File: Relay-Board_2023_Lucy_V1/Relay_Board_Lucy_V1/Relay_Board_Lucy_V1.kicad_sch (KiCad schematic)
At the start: 54 parts, among them J1 VP0265540000G, J2 VP0265540000G, J3 Startup Resistor, J5 Battery Power, J9 VP0265540000G, Q1 SI2302A-TPMSCT-ND, U1 TSV914IPT, U2 ACS770LCB-050U-PFF, U3 ACS770LCB-050U-PFF, U4 ACS770LCB-050U-PFF, U6 MAX14572, U8 TSV914IPT

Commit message: Updates
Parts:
- removed J3: Startup Resistor, symbol Connector:Screw_Terminal_01x02
- added J4: VP0265540000G, RB_FTP:CONN_VP0265x4xxxxG_AMP, symbol RB_PARTS:VP0265540000G
- added NT1: NetTie_2, NetTie:NetTie-2_SMD_Pad2.0mm, symbol Device:NetTie_2
- C9: value 0u1 -> 100n; footprint (none) -> Capacitor_SMD:C_0603_1608Metric
- C9: footprint (none) -> Capacitor_SMD:C_0603_1608Metric
- D1: renamed from D2; footprint (none) -> LED_SMD:LED_0805_2012Metric
- R1: footprint (none) -> Resistor_SMD:R_0603_1608Metric
- renumbered D14 to D10, D15 to D11, D16 to D2, D1 to D3, D7 to D5, D11 to D6, D12 to D7, D13 to D9, J5 to J1, J9 to J2, J1 to J3, J2 to J5, U2 to U1, U3 to U2, U8 to U4, U1 to U5, U4 to U6
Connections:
- net GNDA: now also NT1.1
- net GNDPWR: now also J4.3, J4.4, NT1.2
- net RES+: now also J4.1, J4.2
- no-connect marks 13 -> 14

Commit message: Started the PCB design work
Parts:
- added H1, H2, H3, H4: MountingHole, MountingHole:MountingHole_3.2mm_M3, symbol Mechanical:MountingHole
- U1, U2, U6: footprint Sensor_Current:Allegro_CB_PFF -> RB_FTP:Allegro_CB_PFF_Adjusted
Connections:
- net PA0 is gone; now on net PA4: D8.3 (K), U4.8 (OUT3), U4.9 (IN3-)
- net PA1 is gone; now on net PA6: D5.3 (K), U4.6 (IN2-), U4.7 (OUT2)
- net PA2 is gone; now on net PA7: D7.3 (K), U5.6 (IN2-), U5.7 (OUT2)
- net PA3 is gone; now on net PA5: D9.3 (K), U5.8 (OUT3), U5.9 (IN3-)
- net CAP+: now also J3.3, J3.4; no longer J3.1, J3.2
- net FC+: now also J2.3, J2.4; no longer J2.1, J2.2
- net GNDA: now also C9.1, C9.2, C9.2, C9.2, C9.2, D1.1 (K), D2.3 (K), J1.2 (Pin_2), J1.5 (Pin_5), R1.1, R1.1, R1.1, U1.2 (GND), U2.2 (GND), U6.15 (EP), U6.2 (GND), U6.7 (GND), U6.8 (~{HVEN})
- net GNDPWR: now also J2.1, J2.2, J3.1, J3.2, J5.1, J5.2; no longer C9.1, C9.2, C9.2, C9.2, C9.2, D1.1 (K), D2.3 (K), J1.2 (Pin_2), J1.5 (Pin_5), J2.3, J2.4, J3.3, J3.4, J5.3, J5.4, R1.1, R1.1, R1.1, U1.2 (GND), U2.2 (GND), U6.15 (EP), U6.2 (GND), U6.7 (GND), U6.8 (~{HVEN})
- net MOTOR+: now also J5.3, J5.4; no longer J5.1, J5.2
- net PA4: no longer D6.3 (K), U5.1 (OUT1), U5.2 (IN1-)
- net PB0: no longer R1.1
- net PB1: no longer R1.2
- net PB2: no longer R1.1
- net PA9 renamed PC4
- net PB3 renamed PB15
- new net PB12: R1.1
- new net PB13: R1.2
- new net PB14: R1.1
- new net PC5: D6.3 (K), U5.1 (OUT1), U5.2 (IN1-)
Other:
- moved on the sheet: C9, D1, D2, J2, J3, Q1, R1, U6

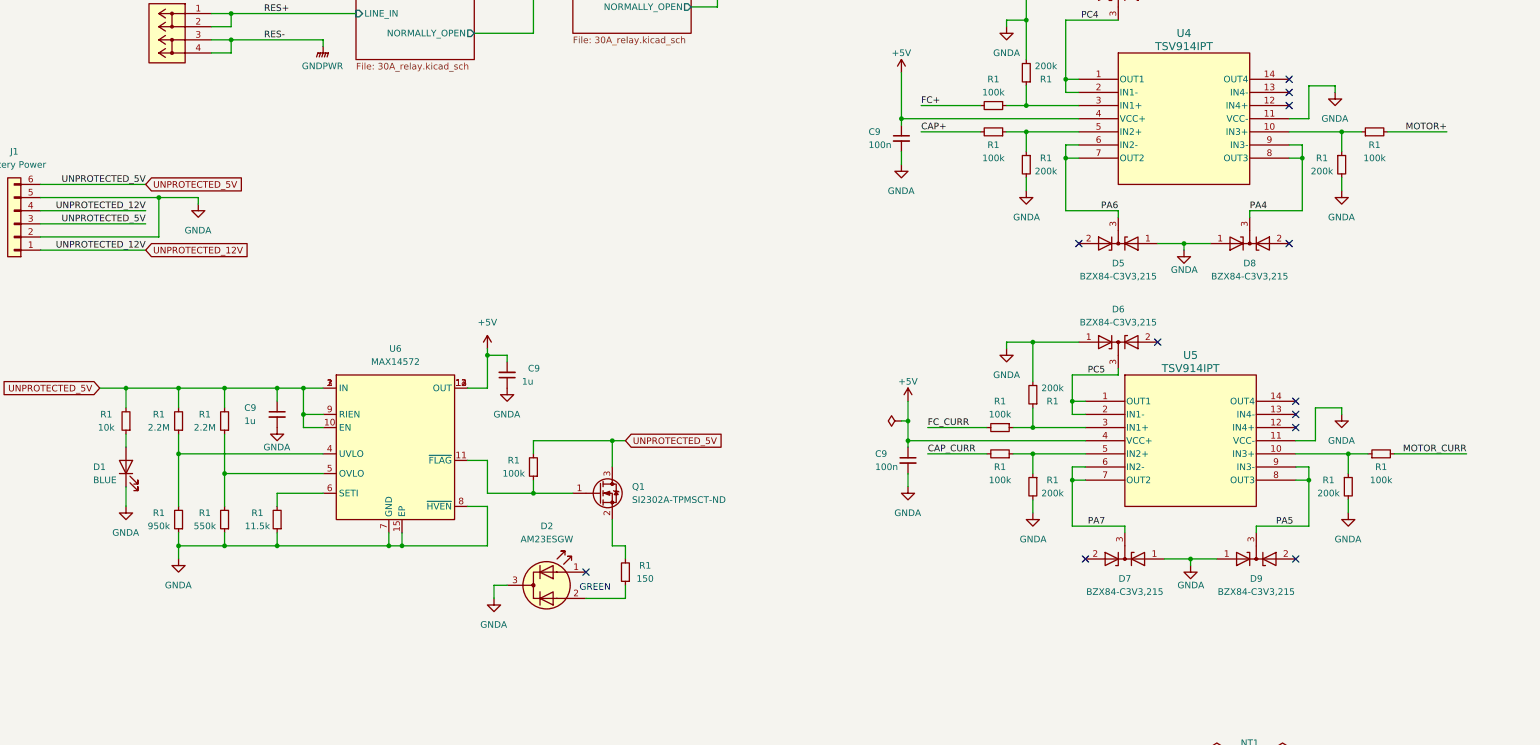
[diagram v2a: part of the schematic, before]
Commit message: Board layout is done and routed
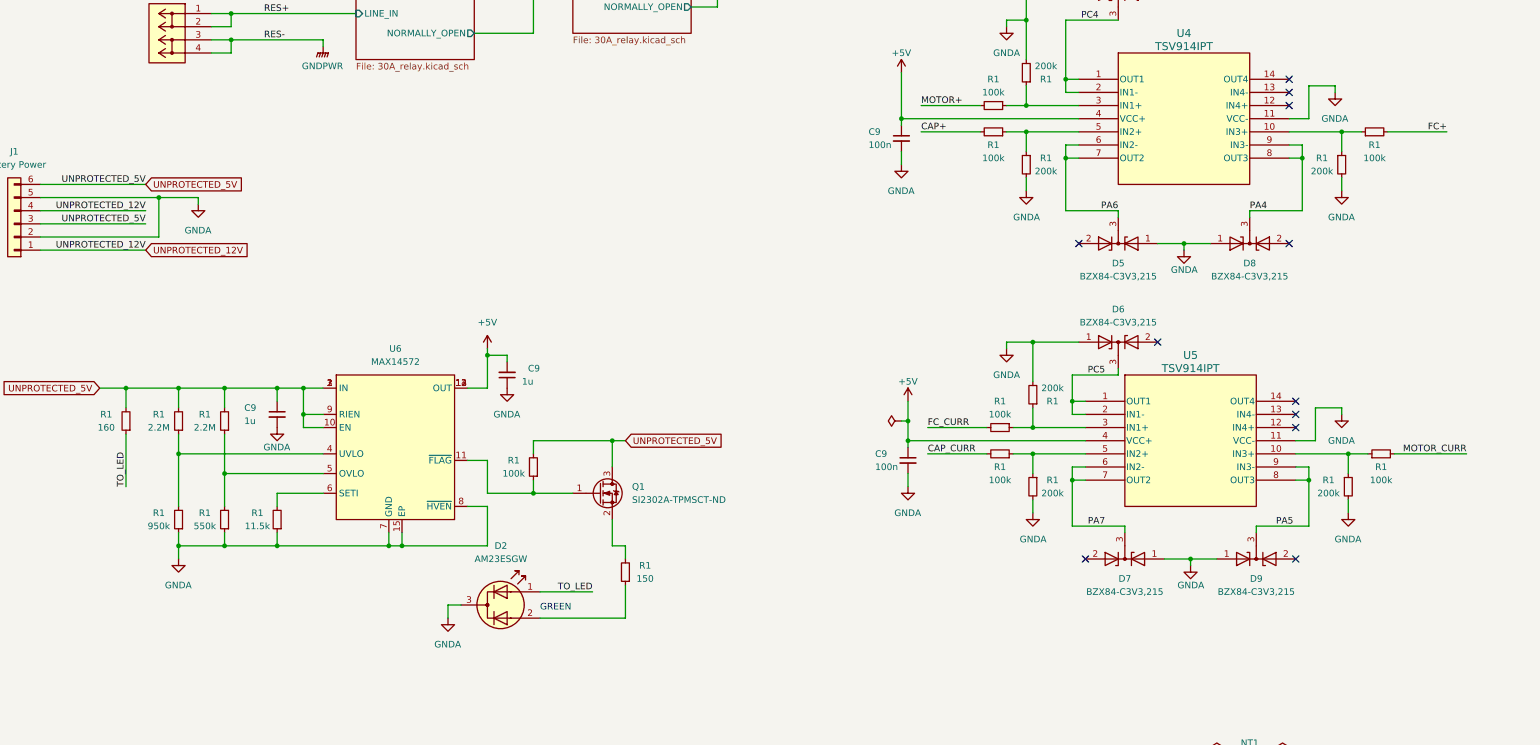
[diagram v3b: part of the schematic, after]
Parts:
- removed D1: BLUE, LED_SMD:LED_0805_2012Metric, symbol Device:LED
- R1: value 10k -> 160
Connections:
- net FC+: now also R1.2; no longer R1.2
- net MOTOR+: now also R1.2; no longer R1.2
- net TO_LED: now reaches R1.1
- net TO_LED: now also D2.1 (A1)
- no-connect marks 14 -> 13
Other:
- moved on the sheet: D2
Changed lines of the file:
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@@
   (no_connect (at 293.37 210.82))
   (no_connect (at 292.1 143.51))
-  (no_connect (at 156.21 238.76))
   (no_connect (at 293.37 236.22))
   (no_connect (at 292.1 175.26))
@@
     (stroke (width 0) (type default))
   )
-  (wire (pts (xy 67.31 212.09) (xy 67.31 214.63))
+  (wire (pts (xy 67.31 212.09) (xy 67.31 222.25))
     (stroke (width 0) (type default))
   )
@@
     (stroke (width 0) (type default))
   )
-  (wire (pts (xy 140.97 241.3) (xy 138.43 241.3))
+  (wire (pts (xy 132.08 245.11) (xy 129.54 245.11))
     (stroke (width 0) (type default))
   )
@@
     (stroke (width 0) (type default))
   )
+  (wire (pts (xy 157.48 242.57) (xy 147.32 242.57))
+    (stroke (width 0) (type default))
+  )
   (wire (pts (xy 262.89 86.36) (xy 257.81 86.36))
     (stroke (width 0) (type default))
@@
     (stroke (width 0) (type default))
   )
-  (wire (pts (xy 138.43 241.3) (xy 138.43 243.84))
+  (wire (pts (xy 129.54 245.11) (xy 129.54 247.65))
     (stroke (width 0) (type default))
   )
@@
     (stroke (width 0) (type default))
   )
-  (wire (pts (xy 156.21 243.84) (xy 163.83 243.84))
+  (wire (pts (xy 147.32 247.65) (xy 163.83 247.65))
     (stroke (width 0) (type default))
   )
@@
     (stroke (width 0) (type default))
   )
-  (wire (pts (xy 67.31 222.25) (xy 67.31 226.06))
-    (stroke (width 0) (type default))
-  )
   (wire (pts (xy 278.13 274.32) (xy 278.13 276.86))
     (stroke (width 0) (type default))
@@
     (stroke (width 0) (type default))
   )
-  (wire (pts (xy 163.83 241.3) (xy 163.83 243.84))
+  (wire (pts (xy 163.83 241.3) (xy 163.83 247.65))
     (stroke (width 0) (type default))
   )
@@
     (effects (font (size 1.27 1.27)) (justify left bottom))
   )
-  (text "GREEN" (at 154.94 242.57 0)
+  (text "GREEN" (at 147.32 246.38 0)
     (effects (font (size 1.27 1.27)) (justify left bottom))
   )
@@
     (effects (font (size 1.27 1.27)) (justify left bottom))
   )
-  (label "FC+" (at 220.98 148.59 0) (fields_autoplaced)
-    (effects (font (size 1.27 1.27)) (justify left bottom))
+  (label "FC+" (at 322.58 153.67 180) (fields_autoplaced)
+    (effects (font (size 1.27 1.27)) (justify right bottom))
   )
   (label "PB12" (at 379.73 41.91 180) (fields_autoplaced)
@@
     (effects (font (size 1.27 1.27)) (justify right bottom))
   )
-  (label "MOTOR+" (at 322.58 153.67 180) (fields_autoplaced)
+  (label "MOTOR+" (at 220.98 148.59 0) (fields_autoplaced)
+    (effects (font (size 1.27 1.27)) (justify left bottom))
+  )
+  (label "TO_LED" (at 157.48 242.57 180) (fields_autoplaced)
     (effects (font (size 1.27 1.27)) (justify right bottom))
   )
@@
   (label "PB13" (at 379.73 46.99 180) (fields_autoplaced)
     (effects (font (size 1.27 1.27)) (justify right bottom))
+  )
+  (label "TO_LED" (at 67.31 222.25 90) (fields_autoplaced)
+    (effects (font (size 1.27 1.27)) (justify left bottom))
   )
   (label "UNPROTECTED_12V" (at 71.12 176.53 180) (fields_autoplaced)
@@
     (property "Intersheetrefs" "${INTERSHEET_REFS}" (at 42.7538 203.2 0)
       (effects (font (size 1.27 1.27)) (justify right) hide)
-    )
-  )
-  (symbol (lib_id "power:GNDA") (at 67.31 226.06 0) (unit 1)
-    (in_bom yes) (on_board yes) (dnp no)
-    (property "Reference" "#PWR023" (at 67.31 232.41 0)
-      (effects (font (size 1.27 1.27)) hide)
-    )
-    (property "Value" "GNDA" (at 69.85 231.14 0)
-      (effects (font (size 1.27 1.27)) (justify right))
-    )
-    (property "Footprint" "" (at 67.31 226.06 0)
-      (effects (font (size 1.27 1.27)) hide)
-    )
-    (property "Datasheet" "" (at 67.31 226.06 0)
-      (effects (font (size 1.27 1.27)) hide)
-    )
-    (pin "1")
-    (instances
-      (project "Relay_Board_Lucy_V1"
-        (path "/1f586fab-d165-4cda-895e-cc224a8182b4/d0430468-7d1b-42a2-a24e-658bd737b804"
-          (reference "#PWR023") (unit 1)
-        )
-        (path "/1f586fab-d165-4cda-895e-cc224a8182b4"
-          (reference "#PWR07") (unit 1)
-        )
-      )
     )
   )
@@
     )
   )
-  (symbol (lib_id "Device:LED") (at 67.31 218.44 90) (unit 1)
-    (in_bom yes) (on_board yes) (dnp no)
-    (property "Reference" "D1" (at 60.96 218.44 90)
-      (effects (font (size 1.27 1.27)) (justify right))
-    )
-    (property "Value" "BLUE" (at 60.96 220.98 90)
-      (effects (font (size 1.27 1.27)) (justify right))
-    )
-    (property "Footprint" "LED_SMD:LED_0805_2012Metric" (at 67.31 218.44 0)
-      (effects (font (size 1.27 1.27)) hide)
-    )
-    (property "Datasheet" "~" (at 67.31 218.44 0)
-      (effects (font (size 1.27 1.27)) hide)
-    )
-    (property "Part#" "" (at 67.31 218.44 0)
-      (effects (font (size 1.27 1.27)) hide)
-    )
-    (pin "1")
-    (pin "2")
-    (instances
-      (project "Relay_Board_Lucy_V1"
-        (path "/1f586fab-d165-4cda-895e-cc224a8182b4"
-          (reference "D1") (unit 1)
-        )
-      )
-    )
-  )
-  (symbol (lib_id "Device:LED_Dual_AAK") (at 148.59 241.3 0) (unit 1)
+  (symbol (lib_id "Device:LED_Dual_AAK") (at 139.7 245.11 0) (unit 1)
     (in_bom yes) (on_board yes) (dnp no) (fields_autoplaced)
-    (property "Reference" "D2" (at 148.6535 229.87 0)
-      (effects (font (size 1.27 1.27)))
-    )
-    (property "Value" "AM23ESGW" (at 148.6535 232.41 0)
-      (effects (font (size 1.27 1.27)))
-    )
-    (property "Footprint" "Package_TO_SOT_SMD:SOT-23-3" (at 148.59 241.3 0)
-      (effects (font (size 1.27 1.27)) hide)
-    )
-    (property "Datasheet" "https://www.kingbrightusa.com/images/catalog/SPEC/AM23ESGW.pdf" (at 148.59 241.3 0)
+    (property "Reference" "D2" (at 139.7635 233.68 0)
+      (effects (font (size 1.27 1.27)))
+    )
+    (property "Value" "AM23ESGW" (at 139.7635 236.22 0)
+      (effects (font (size 1.27 1.27)))
+    )
+    (property "Footprint" "Package_TO_SOT_SMD:SOT-23-3" (at 139.7 245.11 0)
+      (effects (font (size 1.27 1.27)) hide)
+    )
+    (property "Datasheet" "https://www.kingbrightusa.com/images/catalog/SPEC/AM23ESGW.pdf" (at 139.7 245.11 0)
       (effects (font (size 1.27 1.27)) hide)
     )
@@
       (effects (font (size 1.27 1.27)))
     )
-    (property "Value" "10k" (at 63.5 210.82 0)
+    (property "Value" "160" (at 63.5 210.82 0)
       (effects (font (size 1.27 1.27)))
     )
@@
     )
   )
-  (symbol (lib_id "power:GNDA") (at 138.43 243.84 0) (unit 1)
-    (in_bom yes) (on_board yes) (dnp no)
-    (property "Reference" "#PWR023" (at 138.43 250.19 0)
-      (effects (font (size 1.27 1.27)) hide)
-    )
-    (property "Value" "GNDA" (at 140.97 248.92 0)
+  (symbol (lib_id "power:GNDA") (at 129.54 247.65 0) (unit 1)
+    (in_bom yes) (on_board yes) (dnp no)
+    (property "Reference" "#PWR023" (at 129.54 254 0)
+      (effects (font (size 1.27 1.27)) hide)
+    )
+    (property "Value" "GNDA" (at 132.08 252.73 0)
       (effects (font (size 1.27 1.27)) (justify right))
     )
-    (property "Footprint" "" (at 138.43 243.84 0)
-      (effects (font (size 1.27 1.27)) hide)
-    )
-    (property "Datasheet" "" (at 138.43 243.84 0)
-      (effects (font (size 1.27 1.27)) hide)
-    )
+    (property "Footprint" "" (at 129.54 247.65 0)
+      (effects (font (size 1.27 1.27)) hide)
+    )
+    (property "Datasheet" "" (at 129.54 247.65 0)
+      (effects (font (size 1.27 1.27)) hide)
+    )

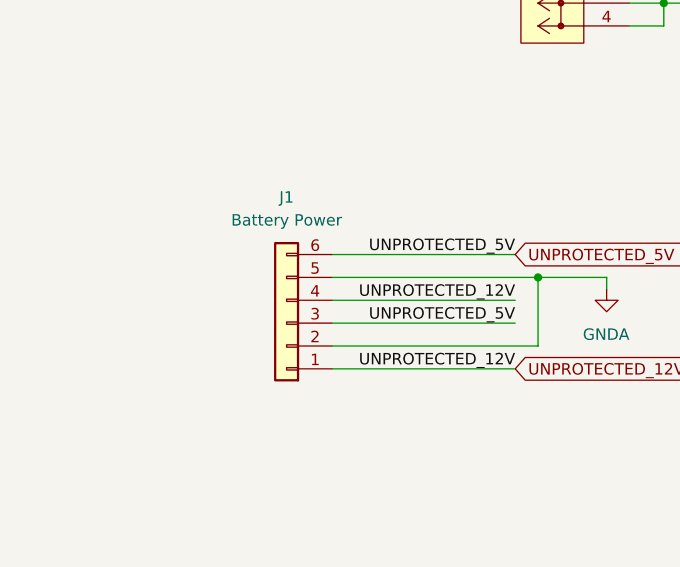
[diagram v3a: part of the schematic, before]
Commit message: Finished the relay board. Once gerbers and drill files are generated we can order from jlc
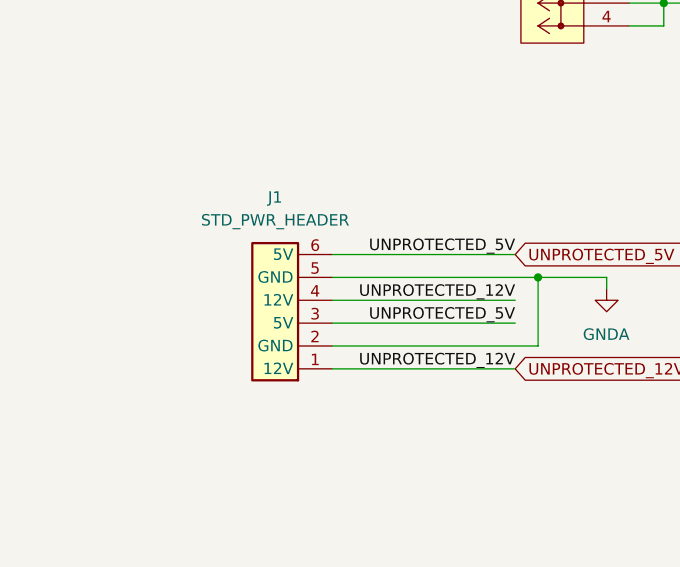
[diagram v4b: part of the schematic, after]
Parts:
- removed J1: Battery Power, Connector_Molex:Molex_Micro-Fit_3.0_43045-0612_2x03_P3.00mm_Vertical, symbol Connector_Generic:Conn_01x06
- added J1: STD_PWR_HEADER, RB_FTP:STD_PWR_HEADER, symbol RB_PARTS:STD_PWR_HEADER
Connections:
- net GNDA: now also J1.2 (GND), J1.5 (GND)
- net UNPROTECTED_12V: now also J1.1 (12V), J1.4 (12V)
- net UNPROTECTED_5V: now also J1.3 (5V), J1.6 (5V)

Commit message: $
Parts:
- added J10: STD_PWR_HEADER, RB_FTP:STD_PWR_HEADER, symbol RB_PARTS:STD_PWR_HEADER
- U2: value ACS770LCB-050U-PFF -> ACS770LCB-050B-PFF
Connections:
- net FC+: now also J10.4 (12V), J10.5 (GND), J10.6 (5V)
- net GNDPWR: now also J10.1 (12V), J10.2 (GND), J10.3 (5V); no longer J4.3, J4.4
- net CAP Charge Relay/NORMALLY_CLOSED renamed TO_CAPS
- new net RES-: J4.3, J4.4
- no-connect marks 13 -> 12
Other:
- sheet CAP Discharge Relay renamed CAP Charge Relay
- note added: "Fuel cell voltage send to the fuel cell power board"
- note added: "Note: The resistor polarity will change during use, thus they are labelled positive and negative solely for naming nets."
- moved on the sheet: J4, R1

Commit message: Started work on the BOM file and I updated the lower current relays to work with 50A models
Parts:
- C9: Part# (none) -> C88219
- C9: Part# (none) -> C77049
- D10, D11, D2, D3, J1, J10, J2, J3, J4, J5, Q1, R1, U1, U2, U6: Part# (none) -> digikey
- D4, D5, D6, D7, D8, D9: Part# (none) -> C85087
- H1, H2, H3, H4, NT1: Part# (none) -> N/A
- R1: Part# (none) -> C209032
- R1: Part# (none) -> C5250829
- R1: Part# (none) -> C5140271
- R1: Part# (none) -> C25811
- R1: Part# (none) -> C22808
- R1: Part# (none) -> C168277
- R1: Part# (none) -> C245189
- R1: Part# (none) -> C304700
- U4, U5: Part# (none) -> C83262
- U6: Part# (none) -> C1519290

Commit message: updated, created gerbers, created p&p, created BOM's
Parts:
- D10, D11, D2: Part# digikey -> 754-1634-6-ND
- D3: Part# digikey -> 497-13279-1-ND
- J1, J10: Part# digikey -> WM1791-ND
- J2, J3, J4, J5: Part# digikey -> VP0265540000G-ND
- Q1: Part# digikey -> SI2302A-TPMSCT-ND
- R1: value 950k -> 953k; Part# digikey -> 311-953KHRCT-ND
- R1: value 100k -> 417k; Part# C5250829 -> 2019-RN73H1JTTD4173C25CT-ND
- R1: value 200k -> 50k; Part# C25811 -> 13-RT0603BRD0750KLCT-ND
- R1: value 550k -> 549k; Part# digikey -> 311-549KHRCT-ND
- U1, U6: Part# digikey -> 620-1542-5-ND
- U2: Part# digikey -> 620-1541-5-ND
- U6: Part# C1519290 -> MAX14572EUD+TCT-ND
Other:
- note added: "Volt Dividers and LP Filters 3.0V = R2/(R1+R2)*28V R2 = 50k R1 = 25/3*R2 = 416k Current to GND is 0.06mA @ 28V"
